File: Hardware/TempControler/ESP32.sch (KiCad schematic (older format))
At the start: 5 parts

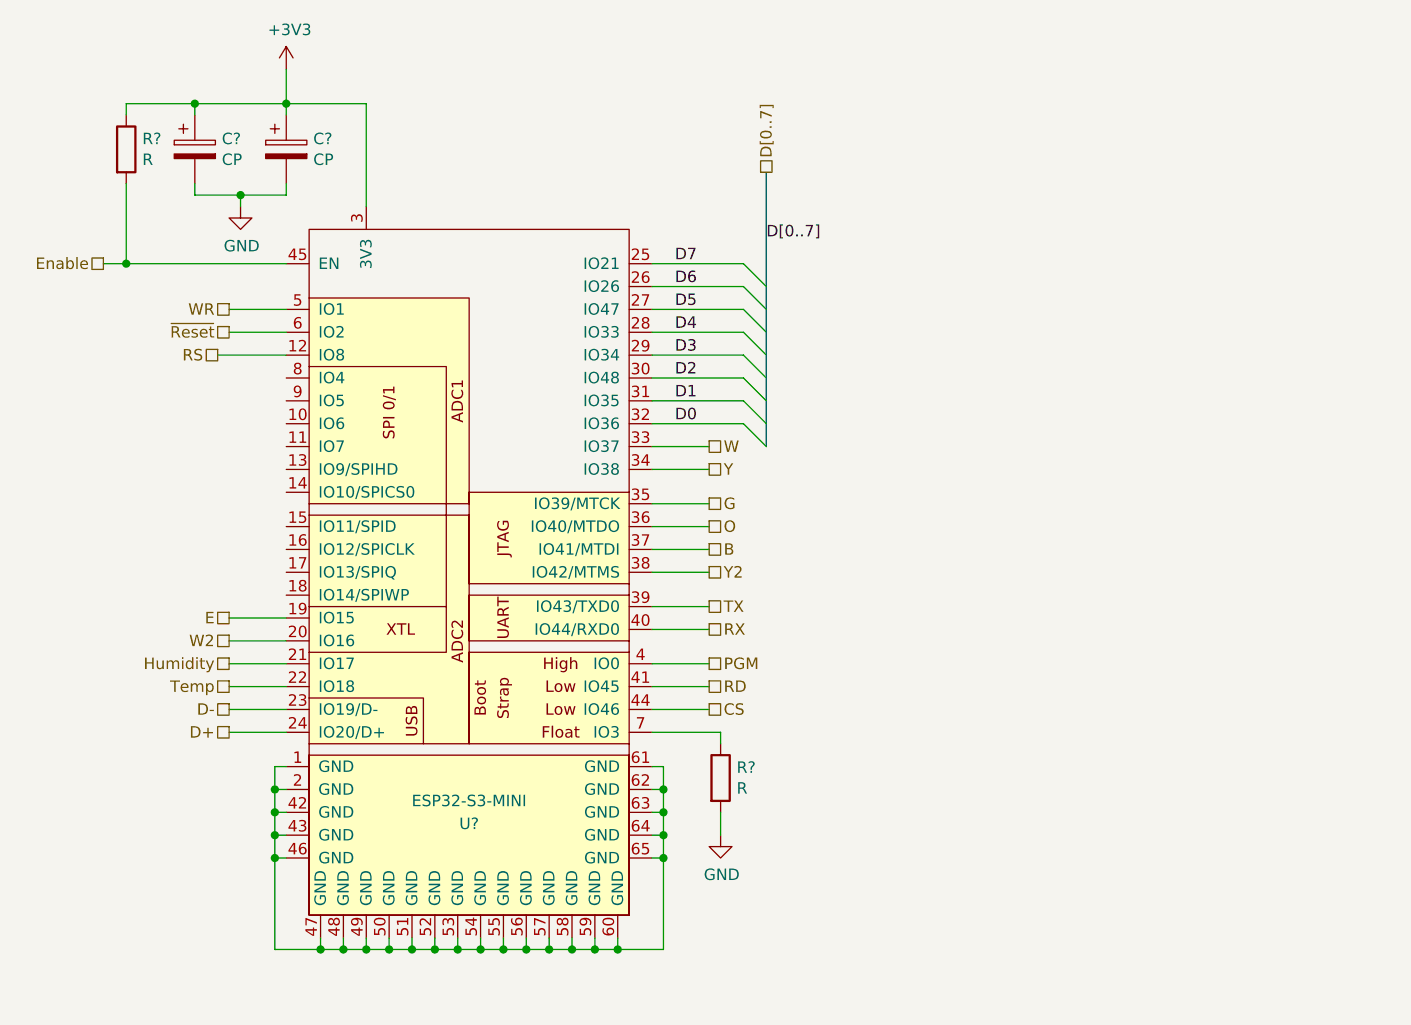
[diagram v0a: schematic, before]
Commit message: Schematic Complete
DRC - Done
Schematic - Done
Values - Done
Part Selection - In Progress
Footprint assignment- In Progress
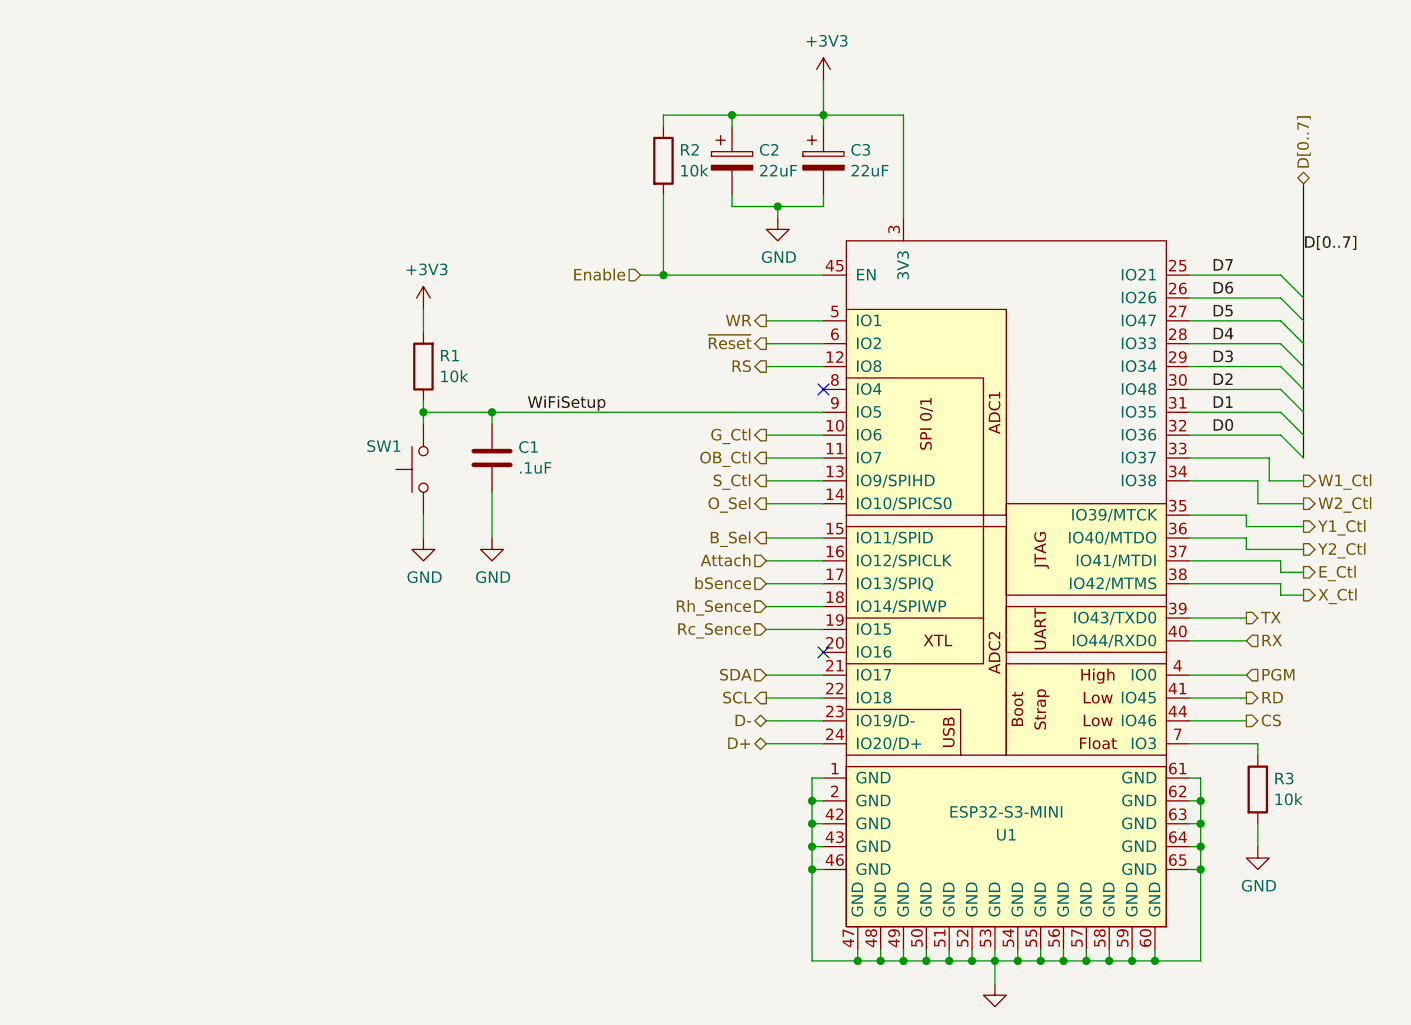
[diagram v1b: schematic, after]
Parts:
- added C1: .1uF, Capacitor_SMD:C_0805_2012Metric, symbol Device:C
- added R1: 10k, Resistor_SMD:R_0603_1608Metric, symbol Device:R
- added SW1: SW_Push, misc:button SMD, symbol Switch:SW_Push
- C2, C3: renamed from C?; value CP -> 22uF; footprint (none) -> Capacitor_SMD:C_0603_1608Metric
- R2, R3: renamed from R?; value R -> 10k; footprint (none) -> Resistor_SMD:R_0603_1608Metric
- gave numbers to parts that had none: 1
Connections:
- net +3V3: now also R1.2
- net GND: now also U1.1 (GND), U1.2 (GND), U1.42 (GND), U1.43 (GND), U1.46 (GND), U1.47 (GND), U1.48 (GND), U1.49 (GND), U1.50 (GND), U1.51 (GND), U1.52 (GND), U1.53 (GND), U1.54 (GND), U1.55 (GND), U1.56 (GND), U1.57 (GND), U1.58 (GND), U1.59 (GND), U1.60 (GND), U1.61 (GND), U1.62 (GND), U1.63 (GND), U1.64 (GND), U1.65 (GND), C1.2, SW1.1
- net G_Ctl: now reaches U1.10 (IO6)
- net OB_Ctl: now reaches U1.11 (IO7)
- net S_Ctl: now reaches U1.13 (IO9/SPIHD)
- net O_Sel: now reaches U1.14 (IO10/SPICS0)
- net B_Sel: now reaches U1.15 (IO11/SPID)
- net Attach: now reaches U1.16 (IO12/SPICLK)
- net bSence: now reaches U1.17 (IO13/SPIQ)
- net Rh_Sence: now reaches U1.18 (IO14/SPIWP)
- net WiFiSetup: now reaches U1.9 (IO5)
- net WiFiSetup: now also C1.1, R1.1, SW1.2
- net B renamed E_Ctl
- net E renamed Rc_Sence
- net G renamed Y1_Ctl
- net Humidity renamed SDA
- net O renamed Y2_Ctl
- net Temp renamed SCL
- net W renamed W1_Ctl
- net W2: no longer names the net of U1.20 (IO16)
- net Y renamed W2_Ctl
- net Y2 renamed X_Ctl
- no-connect marks 0 -> 2
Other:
- moved on the sheet: C2, C3, R2, R3, U1

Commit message: All Part Numbers Selected
Next step select all footprints
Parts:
- C1: Mouser (none) -> 80-C0805C104K5R
- C2, C3: Mouser (none) -> 603-CC0603MPX5R6B226
- R1, R2, R3: Mouser (none) -> 667-ERJ-3EKF1002V
- SW1: Mouser (none) -> 612-LL3301NF065QG
- U1: Mouser (none) -> 356-ESP32-S3-MINI1N8
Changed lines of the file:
@@
 F 1 "22uF" H 3768 1155 50  0000 L CNN
 F 2 "Capacitor_SMD:C_0603_1608Metric" H 3688 1050 50  0001 C CNN
-F 3 "~" H 3650 1200 50  0001 C CNN
+F 3 "https://www.mouser.com/datasheet/2/447/yago_s_a0011397150_1-2286655.pdf" H 3650 1200 50  0001 C CNN
+F 4 "603-CC0603MPX5R6B226" H 3650 1200 50  0001 C CNN "Mouser"
 	1    3650 1200
 	1    0    0    -1
@@
 F 1 "22uF" H 4168 1155 50  0000 L CNN
 F 2 "Capacitor_SMD:C_0603_1608Metric" H 4088 1050 50  0001 C CNN
-F 3 "~" H 4050 1200 50  0001 C CNN
+F 3 "https://www.mouser.com/datasheet/2/447/yago_s_a0011397150_1-2286655.pdf" H 4050 1200 50  0001 C CNN
+F 4 "603-CC0603MPX5R6B226" H 4050 1200 50  0001 C CNN "Mouser"
 	1    4050 1200
 	1    0    0    -1
@@
 F 1 "10k" H 3420 1155 50  0000 L CNN
 F 2 "Resistor_SMD:R_0603_1608Metric" V 3280 1200 50  0001 C CNN
-F 3 "~" H 3350 1200 50  0001 C CNN
+F 3 "https://www.mouser.com/datasheet/2/315/AOA0000C304-1149620.pdf" H 3350 1200 50  0001 C CNN
+F 4 "667-ERJ-3EKF1002V" H 3350 1200 50  0001 C CNN "Mouser"
 	1    3350 1200
 	1    0    0    -1
@@
 F 4 "https://espressif.com/sites/default/files/documentation/esp32-s3_datasheet_en.pdf" H 5000 2550 50  0001 C CNN "ESP32-A3 Datasheet"
 F 5 "https://www.espressif.com/sites/default/files/documentation/esp32-s3_technical_reference_manual_en.pdf" H 4850 2450 50  0001 C CNN "Tech Ref"
+F 6 "356-ESP32-S3-MINI1N8" H 5000 1750 50  0001 C CNN "Mouser"
 	1    5000 1750
 	1    0    0    -1
@@
 F 1 "10k" H 6020 3905 50  0000 L CNN
 F 2 "Resistor_SMD:R_0603_1608Metric" V 5880 3950 50  0001 C CNN
-F 3 "~" H 5950 3950 50  0001 C CNN
+F 3 "https://www.mouser.com/datasheet/2/315/AOA0000C304-1149620.pdf" H 5950 3950 50  0001 C CNN
+F 4 "667-ERJ-3EKF1002V" H 5950 3950 50  0001 C CNN "Mouser"
 	1    5950 3950
 	1    0    0    -1
@@
 F 1 "10k" H 2230 2145 50  0000 R CNN
 F 2 "Resistor_SMD:R_0603_1608Metric" V 2230 2100 50  0001 C CNN
-F 3 "~" H 2300 2100 50  0001 C CNN
+F 3 "https://www.mouser.com/datasheet/2/315/AOA0000C304-1149620.pdf" H 2300 2100 50  0001 C CNN
+F 4 "667-ERJ-3EKF1002V" H 2300 2100 50  0001 C CNN "Mouser"
 	1    2300 2100
 	-1   0    0    1
@@
 F 1 "SW_Push" V 2255 2502 50  0001 R CNN
 F 2 "misc:button SMD" H 2300 2750 50  0001 C CNN
-F 3 "~" H 2300 2750 50  0001 C CNN
+F 3 "https://www.mouser.com/datasheet/2/140/P090002-267756.pdf" H 2300 2750 50  0001 C CNN
+F 4 "612-LL3301NF065QG" H 2300 2550 50  0001 C CNN "Mouser"
 	1    2300 2550
 	0    -1   -1   0
@@
 F 1 ".1uF" H 2715 2455 50  0000 L CNN
 F 2 "Capacitor_SMD:C_0805_2012Metric" H 2638 2350 50  0001 C CNN
-F 3 "~" H 2600 2500 50  0001 C CNN
+F 3 "https://www.mouser.com/datasheet/2/212/KEM_C1002_X7R_SMD-1102033.pdf" H 2600 2500 50  0001 C CNN
+F 4 "80-C0805C104K5R" H 2600 2500 50  0001 C CNN "Mouser"
 	1    2600 2500
 	1    0    0    -1

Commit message: Footprints selected
On to board design
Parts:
- U1: footprint (none) -> ESP32:ESP32-S3-MINI-1
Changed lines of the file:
@@
 F 0 "U1" H 4850 -650 50  0000 C CNN
 F 1 "ESP32­S3­MINI" H 4850 -550 50  0000 C CNN
-F 2 "" H 4850 350 50  0001 C CNN
+F 2 "ESP32:ESP32-S3-MINI-1" H 4850 350 50  0001 C CNN
 F 3 "https://www.mouser.com/datasheet/2/891/esp32_s3_mini_1_mini_1u_datasheet_en-2997643.pdf" H 4850 350 50  0001 C CNN
 F 4 "https://espressif.com/sites/default/files/documentation/esp32-s3_datasheet_en.pdf" H 5000 2550 50  0001 C CNN "ESP32-A3 Datasheet"
